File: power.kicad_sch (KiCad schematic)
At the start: 57 parts

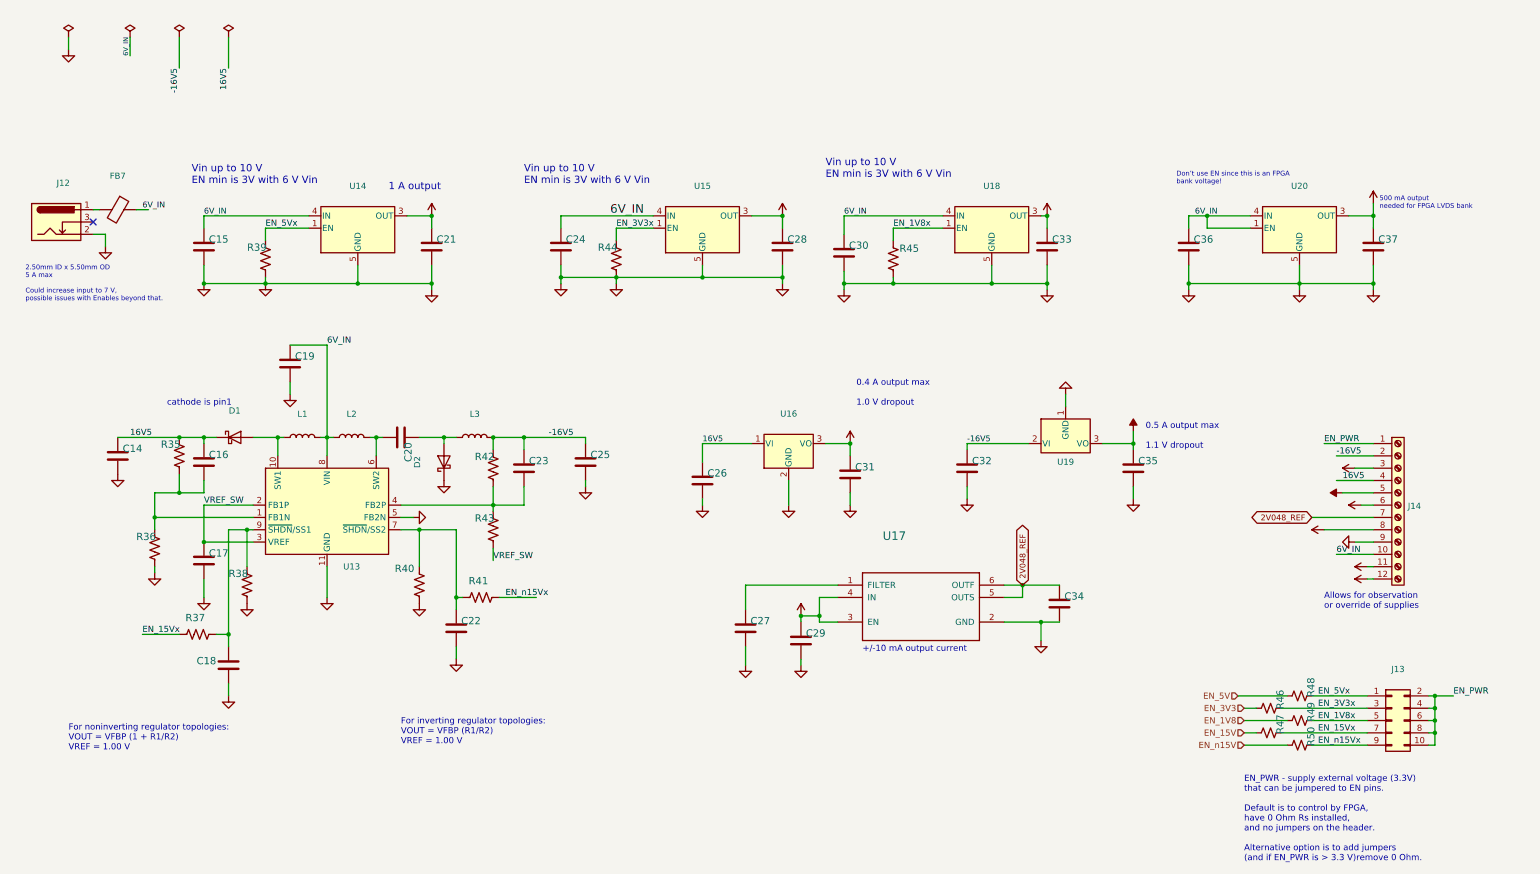
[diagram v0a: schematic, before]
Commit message: closes #31 - incorrect text on Howland current pump. Also, updated fast DAC symbol but not closing until layout is corrected
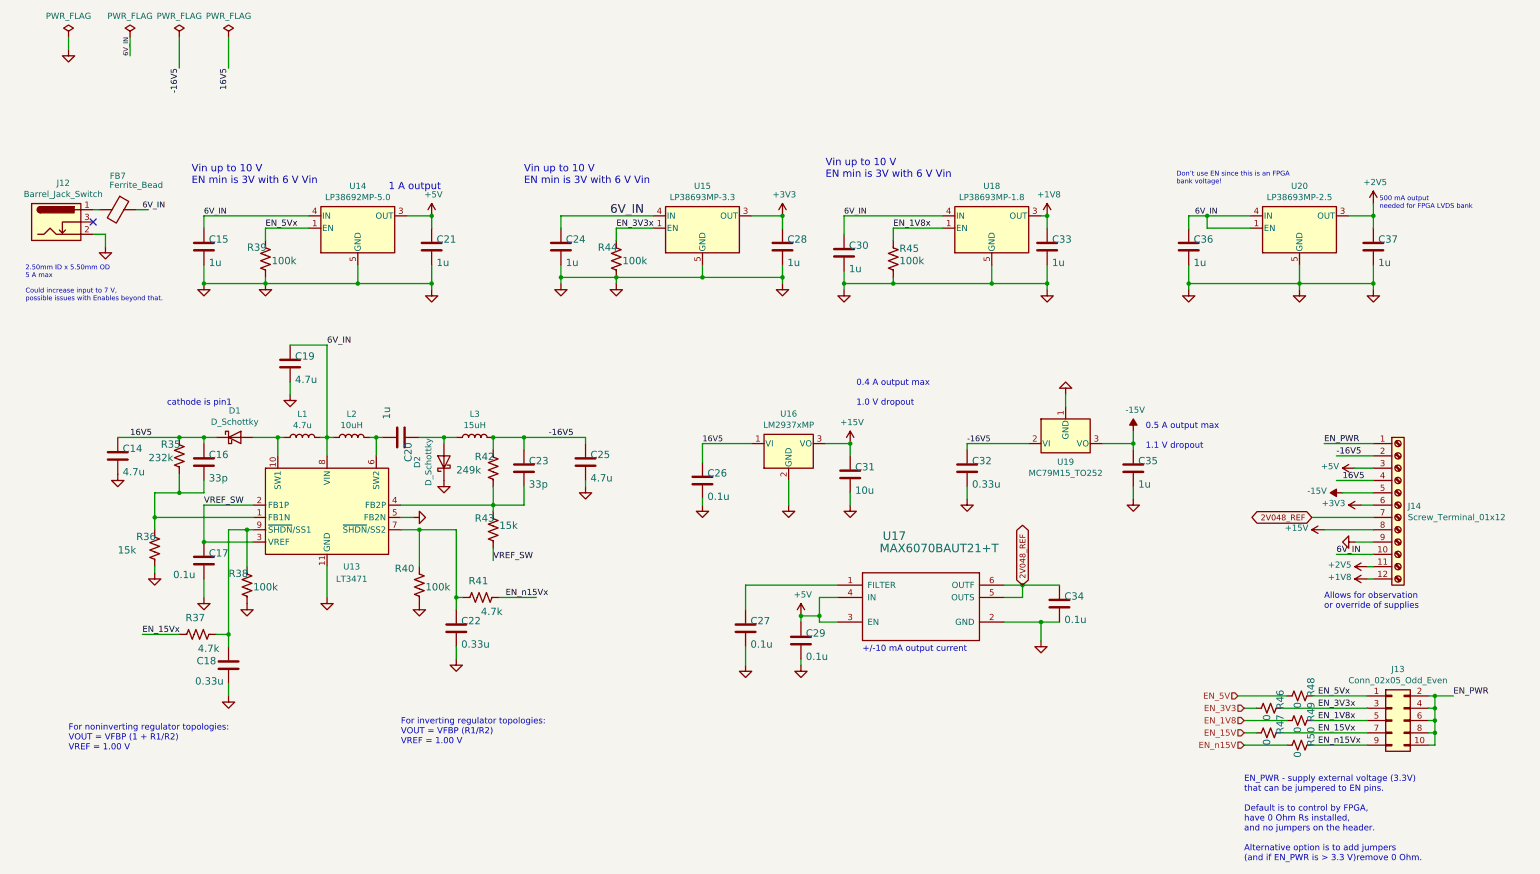
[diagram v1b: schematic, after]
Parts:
- C14, C19, C25: value (none) -> 4.7u; footprint (none) -> Capacitor_SMD:C_0603_1608Metric
- C15, C20, C21, C24, C28, C30, C33, C35, C36, C37: value (none) -> 1u; footprint (none) -> Capacitor_SMD:C_0603_1608Metric
- C16, C23: value (none) -> 33p; footprint (none) -> Capacitor_SMD:C_0603_1608Metric
- C17, C26, C27, C29, C34: value (none) -> 0.1u; footprint (none) -> Capacitor_SMD:C_0603_1608Metric
- C18, C22, C32: value (none) -> 0.33u; footprint (none) -> Capacitor_SMD:C_0603_1608Metric
- C31: value (none) -> 10u; footprint (none) -> Capacitor_SMD:C_0805_2012Metric
- D1, D2: value (none) -> D_Schottky; footprint (none) -> Diode_SMD:D_Powermite_AK
- FB7: value (none) -> Ferrite_Bead; footprint (none) -> Capacitor_SMD:C_1206_3216Metric
- J12: value (none) -> Barrel_Jack_Switch; footprint (none) -> covg-kicad:CUI_PJ-002BH
- J13: value (none) -> Conn_02x05_Odd_Even; footprint (none) -> Connector_PinHeader_2.00mm:PinHeader_2x05_P2.00mm_Vertical_SMD
- J14: value (none) -> Screw_Terminal_01x12; footprint (none) -> TerminalBlock_Phoenix:TerminalBlock_Phoenix_MPT-0,5-12-2.54_1x12_P2.54mm_Horizontal
- L1: value (none) -> 4.7u; footprint (none) -> covg-kicad:SRR4018-4R7Y
- L2: value (none) -> 10uH; footprint (none) -> covg-kicad:NRS5020T100MMGJ
- L3: value (none) -> 15uH; footprint (none) -> covg-kicad:SRR6028-150Y
- R35: value (none) -> 232k; footprint (none) -> Resistor_SMD:R_0603_1608Metric
- R36, R43: value (none) -> 15k; footprint (none) -> Resistor_SMD:R_0603_1608Metric
- R37, R41: value (none) -> 4.7k; footprint (none) -> Resistor_SMD:R_0603_1608Metric
- R38, R39, R40, R44, R45: value (none) -> 100k; footprint (none) -> Resistor_SMD:R_0603_1608Metric
- R42: value (none) -> 249k; footprint (none) -> Resistor_SMD:R_0603_1608Metric
- R46, R47, R48, R49, R50: value (none) -> 0; footprint (none) -> Resistor_SMD:R_0603_1608Metric
- U13: value (none) -> LT3471; footprint (none) -> covg-kicad:DFN-10-1EP_3x3mm_P0.5mm_EP1.65x2.38mm
- U14: value (none) -> LP38692MP-5.0; footprint (none) -> Package_TO_SOT_SMD:SOT-223-5
- U15: value (none) -> LP38693MP-3.3; footprint (none) -> Package_TO_SOT_SMD:SOT-223-5
- U16: value (none) -> LM2937xMP; footprint (none) -> Package_TO_SOT_SMD:SOT-223-3_TabPin2
- U17: value (none) -> MAX6070BAUT21+T; footprint (none) -> Package_TO_SOT_SMD:SOT-23-6_Handsoldering
- U18: value (none) -> LP38693MP-1.8; footprint (none) -> Package_TO_SOT_SMD:SOT-223-5
- U19: value (none) -> MC79M15_TO252; footprint (none) -> Package_TO_SOT_SMD:TO-252-2
- U20: value (none) -> LP38693MP-2.5; footprint (none) -> Package_TO_SOT_SMD:SOT-223-5

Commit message: Closes #37 and Closes #25
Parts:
- C20: value 1u -> (none); footprint Capacitor_SMD:C_0603_1608Metric -> (none)
- D1, D2: value D_Schottky -> (none); footprint Diode_SMD:D_Powermite_AK -> (none)
- L1: value 4.7u -> (none); footprint covg-kicad:SRR4018-4R7Y -> (none)
- L2: value 10uH -> (none); footprint covg-kicad:NRS5020T100MMGJ -> (none)
- L3: value 15uH -> (none); footprint covg-kicad:SRR6028-150Y -> (none)
- R35: value 232k -> (none); footprint Resistor_SMD:R_0603_1608Metric -> (none)
- R42: value 249k -> (none); footprint Resistor_SMD:R_0603_1608Metric -> (none)
- U13: value LT3471 -> (none); footprint covg-kicad:DFN-10-1EP_3x3mm_P0.5mm_EP1.65x2.38mm -> (none)
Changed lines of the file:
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@@
       (effects (font (size 1.4986 1.4986)) (justify left bottom))
     )
-    (property "Value" "249k" (id 1) (at 102.87 111.76 0)
-      (effects (font (size 1.4986 1.4986)) (justify left bottom))
-    )
-    (property "Footprint" "Resistor_SMD:R_0603_1608Metric" (id 2) (at 110.49 110.49 0)
+    (property "Value" "" (id 1) (at 102.87 111.76 0)
+      (effects (font (size 1.4986 1.4986)) (justify left bottom))
+    )
+    (property "Footprint" "" (id 2) (at 110.49 110.49 0)
       (effects (font (size 1.27 1.27)) hide)
     )
@@
     (in_bom yes) (on_board yes)
     (property "Reference" "U13" (id 0) (at 81.28 130.81 0))
-    (property "Value" "LT3471" (id 1) (at 81.28 133.35 0))
-    (property "Footprint" "covg-kicad:DFN-10-1EP_3x3mm_P0.5mm_EP1.65x2.38mm" (id 2) (at 76.2 130.81 0)
+    (property "Value" "" (id 1) (at 81.28 133.35 0))
+    (property "Footprint" "" (id 2) (at 76.2 130.81 0)
       (effects (font (size 1.27 1.27)) hide)
     )
@@
     (in_bom yes) (on_board yes)
     (property "Reference" "L1" (id 0) (at 71.12 99.314 90))
-    (property "Value" "4.7u" (id 1) (at 71.12 101.6254 90))
-    (property "Footprint" "covg-kicad:SRR4018-4R7Y" (id 2) (at 71.12 104.14 0)
+    (property "Value" "" (id 1) (at 71.12 101.6254 90))
+    (property "Footprint" "" (id 2) (at 71.12 104.14 0)
       (effects (font (size 1.27 1.27)) hide)
     )
@@
     (in_bom yes) (on_board yes)
     (property "Reference" "L2" (id 0) (at 81.28 99.314 90))
-    (property "Value" "10uH" (id 1) (at 81.28 101.6254 90))
-    (property "Footprint" "covg-kicad:NRS5020T100MMGJ" (id 2) (at 81.28 104.14 0)
+    (property "Value" "" (id 1) (at 81.28 101.6254 90))
+    (property "Footprint" "" (id 2) (at 81.28 104.14 0)
       (effects (font (size 1.27 1.27)) hide)
     )
@@
     (in_bom yes) (on_board yes)
     (property "Reference" "D1" (id 0) (at 57.15 98.6282 0))
-    (property "Value" "D_Schottky" (id 1) (at 57.15 100.9396 0))
-    (property "Footprint" "Diode_SMD:D_Powermite_AK" (id 2) (at 57.15 104.14 0)
+    (property "Value" "" (id 1) (at 57.15 100.9396 0))
+    (property "Footprint" "" (id 2) (at 57.15 104.14 0)
       (effects (font (size 1.27 1.27)) hide)
     )
@@
       (effects (font (size 1.4986 1.4986)) (justify left bottom))
     )
-    (property "Value" "232k" (id 1) (at 39.37 109.22 0)
-      (effects (font (size 1.4986 1.4986)) (justify left bottom))
-    )
-    (property "Footprint" "Resistor_SMD:R_0603_1608Metric" (id 2) (at 45.72 107.95 0)
+    (property "Value" "" (id 1) (at 39.37 109.22 0)
+      (effects (font (size 1.4986 1.4986)) (justify left bottom))
+    )
+    (property "Footprint" "" (id 2) (at 45.72 107.95 0)
       (effects (font (size 1.27 1.27)) hide)
     )
@@
       (effects (font (size 1.4986 1.4986)) (justify left bottom))
     )
-    (property "Value" "1u" (id 1) (at 87.63 97.79 0)
-      (effects (font (size 1.4986 1.4986)) (justify left bottom))
-    )
-    (property "Footprint" "Capacitor_SMD:C_0603_1608Metric" (id 2) (at 91.44 104.14 0)
+    (property "Value" "" (id 1) (at 87.63 97.79 0)
+      (effects (font (size 1.4986 1.4986)) (justify left bottom))
+    )
+    (property "Footprint" "" (id 2) (at 91.44 104.14 0)
       (effects (font (size 1.27 1.27)) hide)
     )
@@
     (in_bom yes) (on_board yes)
     (property "Reference" "D2" (id 0) (at 94.8182 109.22 0))
-    (property "Value" "D_Schottky" (id 1) (at 97.1296 109.22 0))
-    (property "Footprint" "Diode_SMD:D_Powermite_AK" (id 2) (at 100.33 109.22 0)
+    (property "Value" "" (id 1) (at 97.1296 109.22 0))
+    (property "Footprint" "" (id 2) (at 100.33 109.22 0)
       (effects (font (size 1.27 1.27)) hide)
     )
@@
     (in_bom yes) (on_board yes)
     (property "Reference" "L3" (id 0) (at 106.68 99.314 90))
-    (property "Value" "15uH" (id 1) (at 106.68 101.6254 90))
-    (property "Footprint" "covg-kicad:SRR6028-150Y" (id 2) (at 106.68 104.14 0)
-      (effects (font (size 1.27 1.27)) hide)
-    )
+    (property "Value" "" (id 1) (at 106.68 101.6254 90))
+    (property "Footprint" "" (id 2) (at 106.68 104.14 0)
+      (effects (font (size 1.27 1.27)) hide)
+    )
